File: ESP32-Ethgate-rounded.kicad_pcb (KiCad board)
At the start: 2 copper layers, 71.2 x 38.1 mm, 56 parts, among them J1 USB_B_Micro, J2 HR911105A, J3 USB, J4 GPIO, Q1 UMH3N, U1 HT7233, U2 ESP32-WROOM-32U, U3 CH340C, U4 HT7233, U5 LAN8720A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

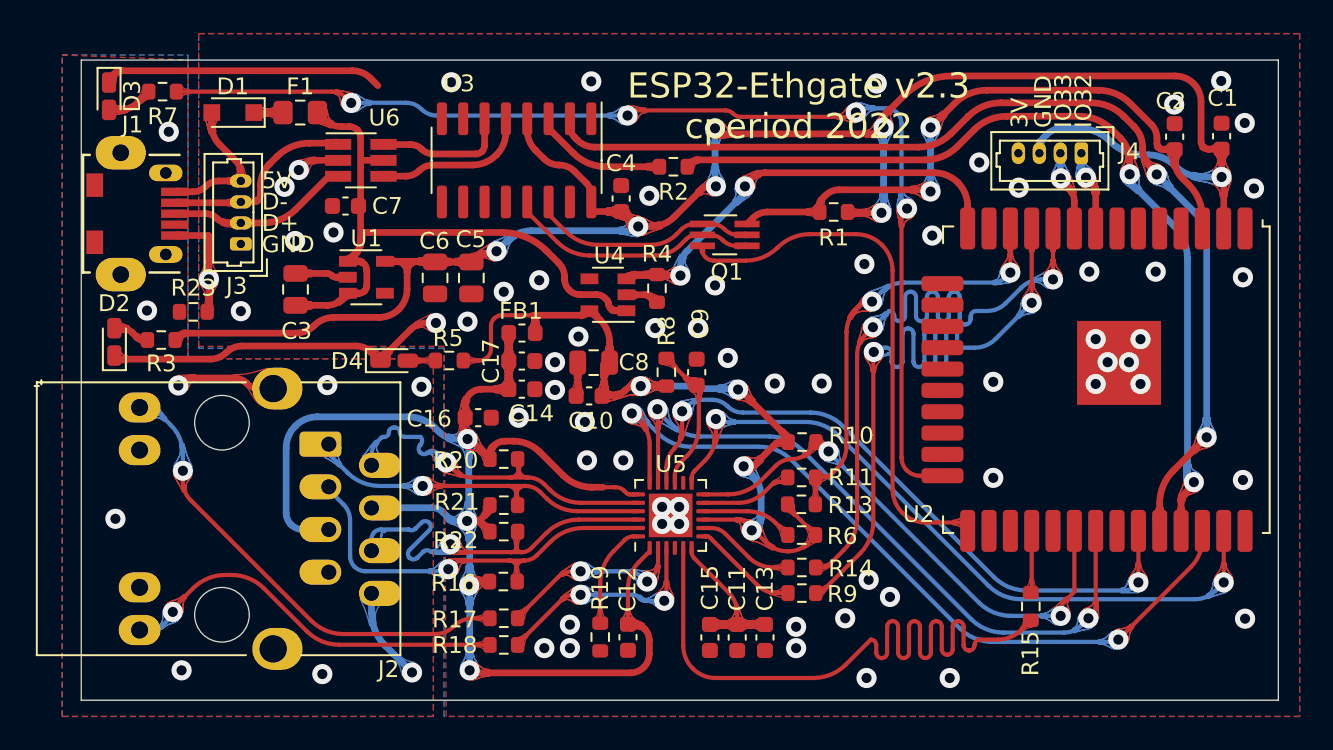
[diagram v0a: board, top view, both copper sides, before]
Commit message: properly fix the nINTSEL for #1 (and document the bootstrap settings in the schematic so I remember next time).
this implicitly updates to Kicad 7.
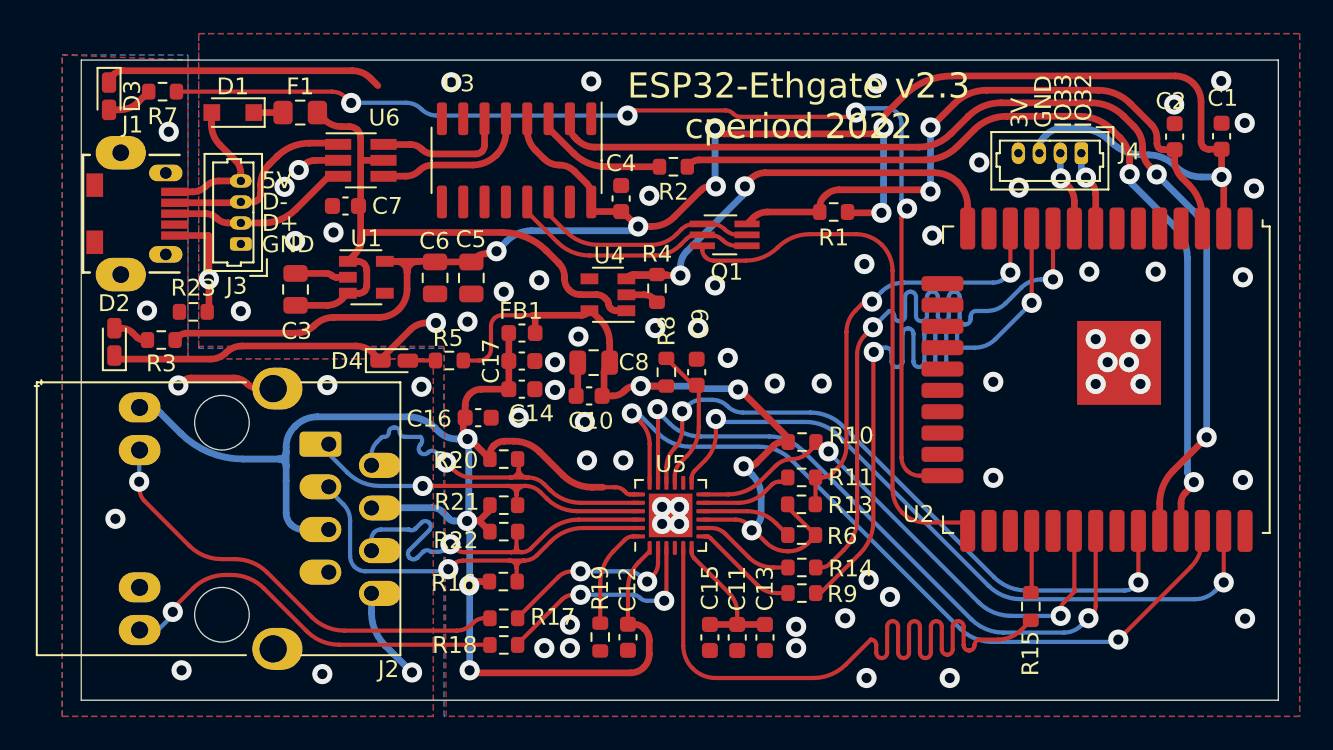
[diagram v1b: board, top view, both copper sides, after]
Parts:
- turned R17 to 0 degrees
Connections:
- J2 pad 10: GND1 -> Net-(J2-Pad10)
- J2 pad 9: Net-(J2-Pad9) -> +3.3VA
- R17 pad 1: /LINKLED -> Net-(J2-Pad10)
- R17 pad 2: Net-(J2-Pad9) -> /LINKLED
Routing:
- net Net-(J2-Pad9): track 27.5 -> 0.00 mm, vias 1 -> 0
- net Net-(J2-Pad10): track 0.00 -> 26.7 mm, vias 0 -> 1
- net +3.3VA: track 82.2 -> 92.8 mm

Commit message: update rev number
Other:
- board text added: "ESP32-Ethgate v2.4 cperiod 2022"
- board text removed: "ESP32-Ethgate v2.3 cperiod 2022"
